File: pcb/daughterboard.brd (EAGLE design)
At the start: 28 x 24 mm, 26 parts, among them IC3 STM32F042F4, SW1 324_SW, SW2 324_SW, SW3 324_SW, SW4 324_SW, SW5 324_SW, SW6 324_SW, U4 XC6206_DEV

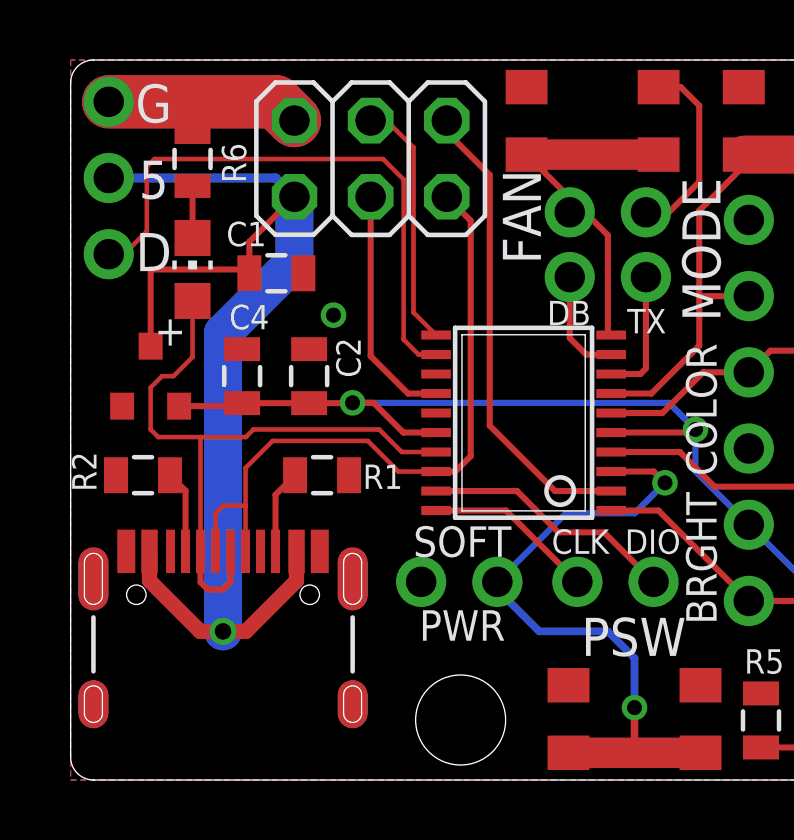
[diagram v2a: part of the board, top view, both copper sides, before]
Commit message: fixed a wrong signal
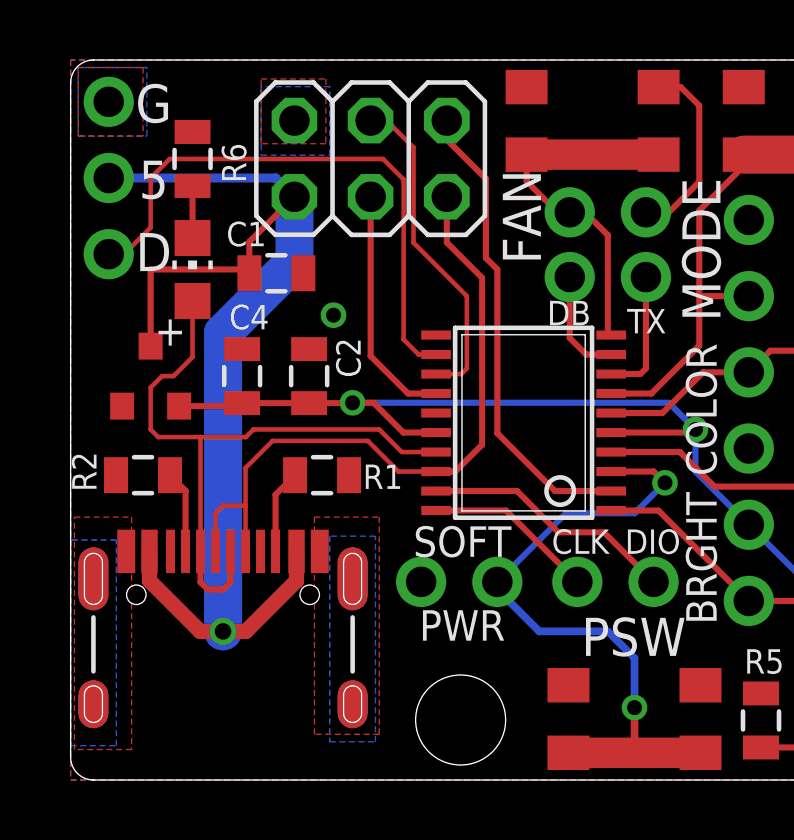
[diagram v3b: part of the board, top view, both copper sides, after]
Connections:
- net N$1: now also IC3.13; no longer IC3.11
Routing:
- net GND: track 19.2 -> 6.35 mm
- net N$1: track 8.36 -> 11.0 mm
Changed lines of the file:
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@@
 <contactref element="J4" pad="GND"/>
 <contactref element="JP3" pad="3"/>
-<wire x1="7.46" y1="21.98" x2="6.834" y2="22.606" width="1.778" layer="1"/>
-<wire x1="6.834" y1="22.606" x2="1.27" y2="22.606" width="1.778" layer="1"/>
-<wire x1="7.46" y1="21.98" x2="6.834" y2="22.606" width="1.778" layer="16"/>
-<wire x1="6.834" y1="22.606" x2="1.27" y2="22.606" width="1.778" layer="16"/>
 <contactref element="SW6" pad="P$3"/>
 <contactref element="SW6" pad="P$2"/>
@@
 </polygon>
 <via x="8.763" y="15.494" extent="1-16" drill="0.5"/>
+<polygon width="0.1524" layer="16" thermals="no">
+<vertex x="0.254" y="21.463"/>
+<vertex x="2.54" y="21.463"/>
+<vertex x="2.54" y="23.749"/>
+<vertex x="0.254" y="23.749"/>
+</polygon>
+<polygon width="0.1524" layer="16" thermals="no">
+<vertex x="6.35" y="20.828"/>
+<vertex x="8.636" y="20.828"/>
+<vertex x="8.636" y="23.114"/>
+<vertex x="6.35" y="23.114"/>
+</polygon>
+<polygon width="0.1524" layer="16" thermals="no">
+<vertex x="8.636" y="1.27"/>
+<vertex x="10.16" y="1.27"/>
+<vertex x="10.16" y="8.128"/>
+<vertex x="8.636" y="8.128"/>
+</polygon>
+<polygon width="0.1524" layer="16" thermals="no">
+<vertex x="0" y="1.143"/>
+<vertex x="1.524" y="1.143"/>
+<vertex x="1.524" y="8.001"/>
+<vertex x="0" y="8.001"/>
+</polygon>
+<polygon width="0.1524" layer="1" thermals="no">
+<vertex x="0.254" y="23.749"/>
+<vertex x="2.413" y="23.749"/>
+<vertex x="2.413" y="21.463"/>
+<vertex x="0.254" y="21.463"/>
+</polygon>
+<polygon width="0.1524" layer="1" thermals="no">
+<vertex x="6.35" y="23.368"/>
+<vertex x="8.509" y="23.368"/>
+<vertex x="8.509" y="21.209"/>
+<vertex x="6.35" y="21.209"/>
+</polygon>
+<polygon width="0.1524" layer="1" thermals="no">
+<vertex x="8.128" y="8.763"/>
+<vertex x="10.287" y="8.763"/>
+<vertex x="10.287" y="1.524"/>
+<vertex x="8.128" y="1.524"/>
+</polygon>
+<polygon width="0.1524" layer="1" thermals="no">
+<vertex x="0.127" y="8.763"/>
+<vertex x="2.032" y="8.763"/>
+<vertex x="2.032" y="1.016"/>
+<vertex x="0.127" y="1.016"/>
+</polygon>
 </signal>
 <signal name="+3V3">
@@
 <contactref element="J4" pad="B6" route="any" routetag="J1.D+"/>
 <contactref element="JP1" pad="5"/>
-<wire x1="12.54" y1="19.44" x2="13.335" y2="18.645" width="0.2032" layer="1"/>
+<wire x1="12.54" y1="19.44" x2="12.54" y2="17.916" width="0.2032" layer="1"/>
+<wire x1="13.716" y1="16.74" x2="12.54" y2="17.916" width="0.2032" layer="1"/>
 <wire x1="12.822" y1="10.282" x2="12.1812" y2="10.282" width="0.2032" layer="1"/>
-<wire x1="13.335" y1="18.645" x2="13.335" y2="10.795" width="0.2032" layer="1"/>
-<wire x1="13.335" y1="10.795" x2="12.822" y2="10.282" width="0.2032" layer="1"/>
+<wire x1="13.716" y1="16.74" x2="13.716" y2="11.176" width="0.2032" layer="1"/>
+<wire x1="13.716" y1="11.176" x2="12.822" y2="10.282" width="0.2032" layer="1"/>
 <wire x1="5.83" y1="7.62" x2="5.83" y2="9.144" width="0.1524" layer="1"/>
 <wire x1="5.83" y1="9.144" x2="5.83" y2="10.402" width="0.1524" layer="1"/>
@@
 <signal name="N$1">
 <contactref element="JP1" pad="4"/>
-<contactref element="IC3" pad="11"/>
-<wire x1="12.1812" y1="14.832" x2="11.43" y2="15.5832" width="0.1524" layer="1"/>
 <wire x1="10.532" y1="21.98" x2="10" y2="21.98" width="0.1524" layer="1"/>
-<wire x1="11.43" y1="15.5832" x2="11.43" y2="21.082" width="0.1524" layer="1"/>
-<wire x1="11.43" y1="21.082" x2="10.532" y2="21.98" width="0.1524" layer="1"/>
+<wire x1="10.532" y1="21.98" x2="11.43" y2="21.082" width="0.1524" layer="1"/>
+<contactref element="IC3" pad="13"/>
+<wire x1="11.43" y1="21.082" x2="11.43" y2="17.907" width="0.1524" layer="1"/>
+<wire x1="11.43" y1="17.907" x2="13.208" y2="16.129" width="0.1524" layer="1"/>
+<wire x1="13.208" y1="16.129" x2="13.208" y2="13.716" width="0.1524" layer="1"/>
+<wire x1="13.024" y1="13.532" x2="12.1812" y2="13.532" width="0.1524" layer="1"/>
+<wire x1="13.208" y1="13.716" x2="13.024" y2="13.532" width="0.1524" layer="1"/>
 </signal>
 <signal name="N$2">
@@
 <contactref element="JP1" pad="6"/>
 <contactref element="IC3" pad="2"/>
-<wire x1="18.0168" y1="9.632" x2="16.149" y2="9.632" width="0.2032" layer="1"/>
-<wire x1="16.149" y1="9.632" x2="13.97" y2="11.811" width="0.2032" layer="1"/>
-<wire x1="13.97" y1="11.811" x2="13.97" y2="20.169" width="0.2032" layer="1"/>
-<wire x1="13.97" y1="20.169" x2="12.54" y2="21.599" width="0.2032" layer="1"/>
-<wire x1="12.54" y1="21.599" x2="12.54" y2="21.98" width="0.2032" layer="1"/>
+<wire x1="16.149" y1="9.632" x2="18.0168" y2="9.632" width="0.2032" layer="1"/>
+<wire x1="13.843" y1="20.042" x2="12.54" y2="21.345" width="0.2032" layer="1"/>
+<wire x1="12.54" y1="21.345" x2="12.54" y2="21.98" width="0.2032" layer="1"/>
+<wire x1="13.843" y1="20.042" x2="13.843" y2="17.399" width="0.2032" layer="1"/>
+<wire x1="14.224" y1="11.557" x2="16.149" y2="9.632" width="0.2032" layer="1"/>
+<wire x1="13.843" y1="17.399" x2="14.224" y2="17.018" width="0.2032" layer="1"/>
+<wire x1="14.224" y1="17.018" x2="14.224" y2="11.557" width="0.2032" layer="1"/>
 </signal>
 <signal name="N$5">
@@
 <wire x1="11.0998" y1="14.6812" x2="11.0998" y2="20.0152" width="0.1524" layer="1"/>
 <wire x1="11.0998" y1="20.0152" x2="10.414" y2="20.701" width="0.1524" layer="1"/>
-<wire x1="10.414" y1="20.701" x2="2.794" y2="20.701" width="0.1524" layer="1"/>
-<wire x1="2.794" y1="20.701" x2="2.54" y2="20.447" width="0.1524" layer="1"/>
-<wire x1="2.54" y1="20.447" x2="2.54" y2="18.288" width="0.1524" layer="1"/>
-<wire x1="2.54" y1="18.288" x2="1.778" y2="17.526" width="0.1524" layer="1"/>
+<wire x1="10.414" y1="20.701" x2="3.302" y2="20.701" width="0.1524" layer="1"/>
+<wire x1="3.302" y1="20.701" x2="2.667" y2="20.066" width="0.1524" layer="1"/>
+<wire x1="2.667" y1="20.066" x2="2.667" y2="18.415" width="0.1524" layer="1"/>
+<wire x1="2.667" y1="18.415" x2="1.778" y2="17.526" width="0.1524" layer="1"/>
 <wire x1="1.778" y1="17.526" x2="1.27" y2="17.526" width="0.1524" layer="1"/>
 </signal>
@@
 <wire x1="17.907" y1="18.161" x2="17.145" y2="18.923" width="0.2032" layer="1"/>
 <wire x1="17.145" y1="18.923" x2="16.637" y2="18.923" width="0.2032" layer="1"/>
-<wire x1="16.637" y1="18.923" x2="16.637" y2="19.408" width="0.2032" layer="1"/>
-<wire x1="16.637" y1="19.408" x2="15.199" y2="20.846" width="0.2032" layer="1"/>
+<wire x1="16.637" y1="18.923" x2="16.233" y2="18.923" width="0.2032" layer="1"/>
+<wire x1="16.233" y1="18.923" x2="15.199" y2="19.957" width="0.2032" layer="1"/>
+<wire x1="15.199" y1="19.957" x2="15.199" y2="20.846" width="0.2032" layer="1"/>
 </signal>
 <signal name="N$10">

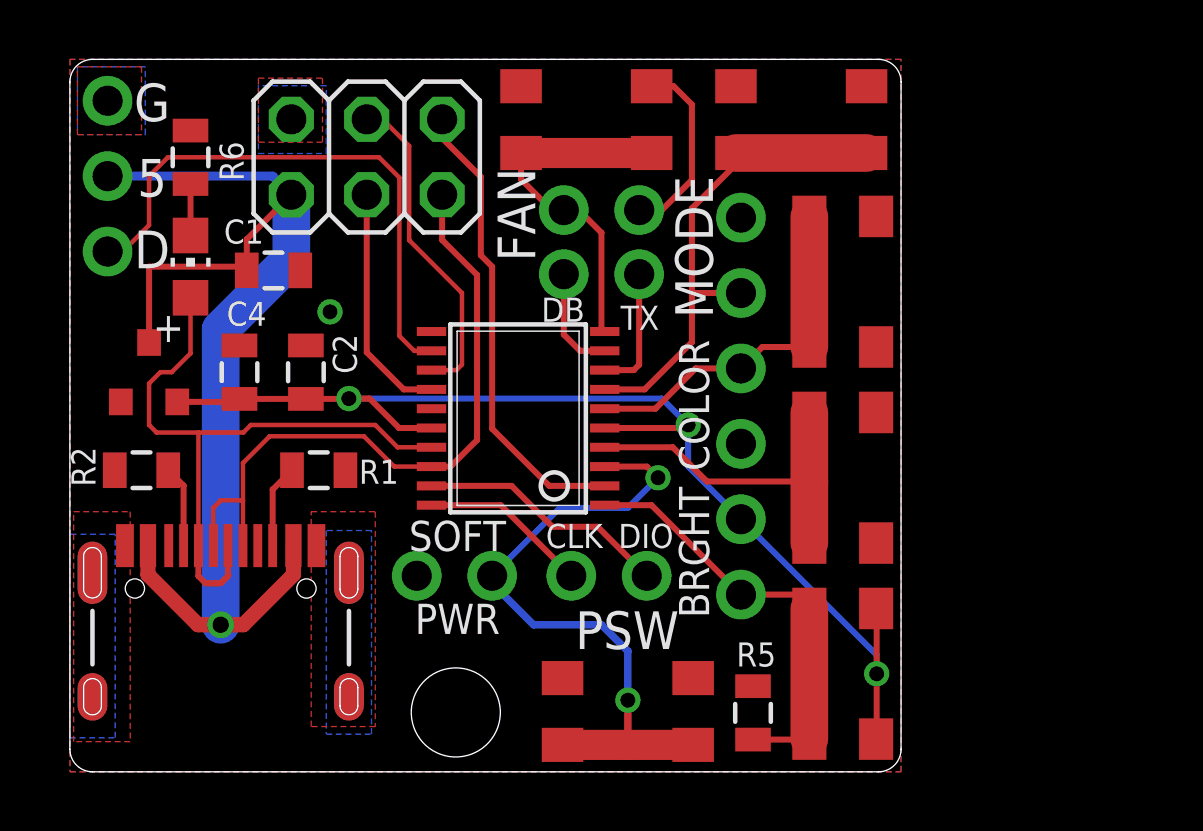
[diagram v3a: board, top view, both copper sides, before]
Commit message: added pullup on 1wire, gnd pour cleanup
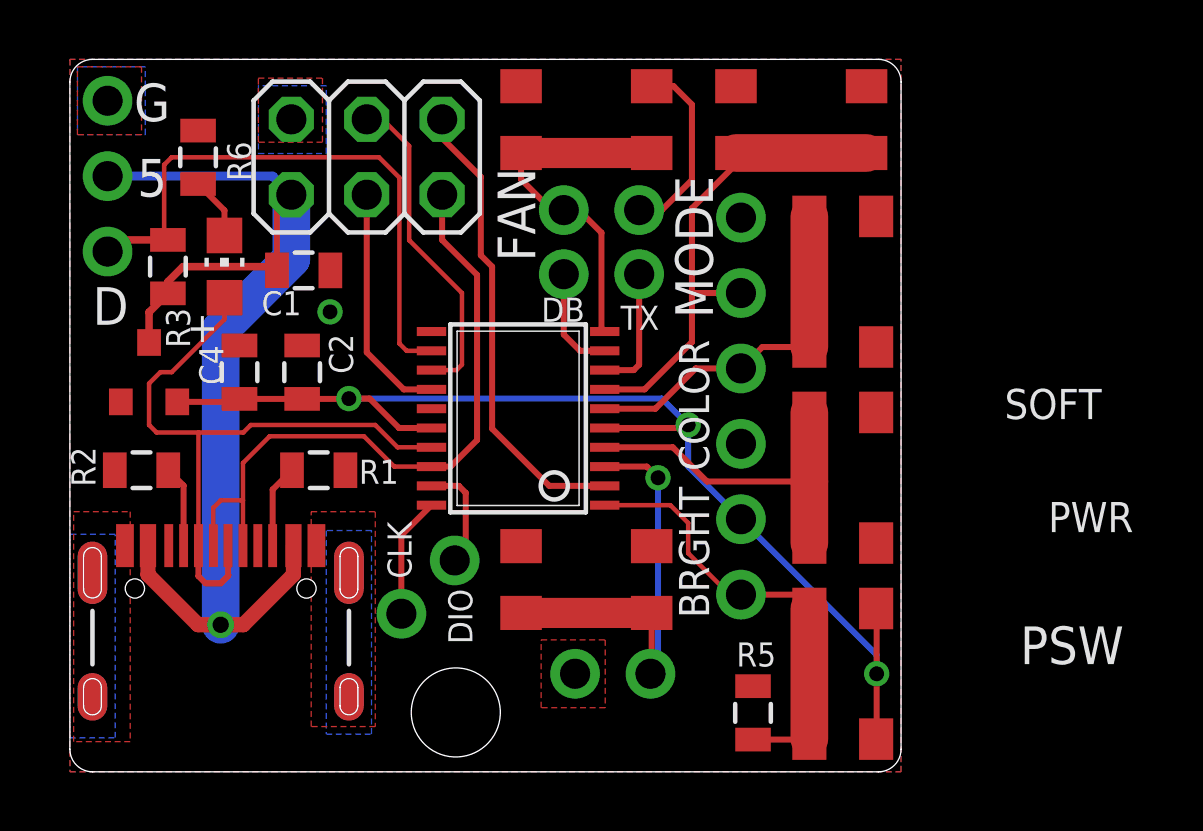
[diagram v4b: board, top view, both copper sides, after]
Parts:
- added R3: 5K1, SparkFun-Passives:0805
- R1, R2, R5: value 5.1K -> 5K1
- R6: value 1K -> 5K1
- moved U$7 6.27 mm to (18.3, 3.30)
- moved U$5 6.11 mm to (12.1, 6.22), turned to 45 degrees
- moved SW6 4.66 mm to (17.4, 6.48)
- moved LED2 1.14 mm to (5.21, 17.0)
- moved C1 1.02 mm to (7.87, 16.9)
- moved R6 0.25 mm to (4.32, 20.7)
- moved C2 0.13 mm to (7.82, 13.5)
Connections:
- net +5V: now also R3.1
- net N$5: now also R3.2
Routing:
- net N$12: track 22.2 -> 15.1 mm, vias 2 -> 1
- net N$3: track 8.50 -> 3.68 mm
- net N$4: track 5.69 -> 4.08 mm
- net N$5: track 19.0 -> 19.8 mm
- net BUTTON2: track 14.6 -> 15.2 mm

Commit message: cleanup
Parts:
- removed SW3: 324_SW, 3pos_slide_switch_centered:342_SWICH_FOOT
- added U$8: PINHD1X2, adafruit_changed:1X02
- moved SW4 3.68 mm to (26.0, 6.99), turned to 270 degrees
- moved R5 3.14 mm to (26.0, 2.82), turned to 180 degrees
- moved U$4 0.51 mm to (22.6, 6.73)
- moved U$5 0.28 mm to (12.2, 6.48)
- moved U$3 0.25 mm to (22.6, 12.1)
- moved U$7 0.25 mm to (18.3, 3.05)
- moved SW6 0.13 mm to (17.4, 6.35)
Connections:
- net BUTTON1: now also U$8.1; no longer SW3.P$2, SW3.P$3
- net GND: now also U$8.2; no longer SW3.P$1, SW3.P$4
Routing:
- net +3V3: track 39.1 -> 35.3 mm, vias 3 -> 2
- net BUTTON2: track 15.2 -> 18.2 mm
- net BUTTON1: track 11.8 -> 9.00 mm
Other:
- board text added: "ATX4VC MCU Board"
- board text added: "DFU"
- board text added: "PD1 APR23"
- board text added: "SOFT PWR"
- board text removed: "ATX4VC Expansion Card"
- board text removed: "PSW"
- board text removed: "PT1 APR23"
- board text removed: "PWR"
- board text removed: "SOFT"

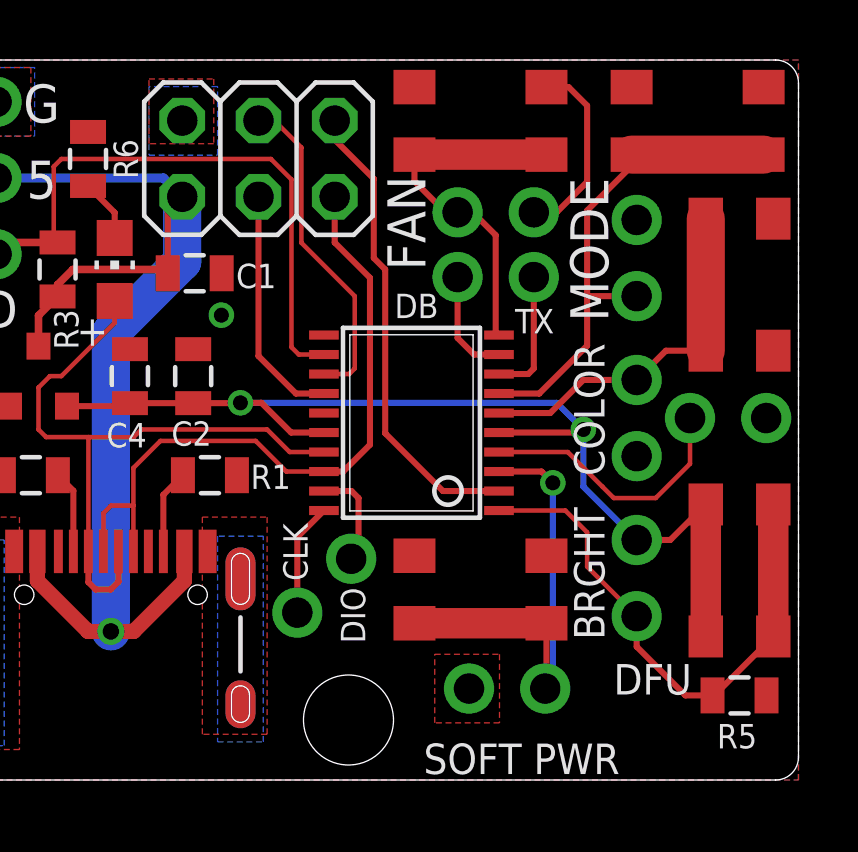
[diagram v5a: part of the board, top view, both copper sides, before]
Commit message: moved pin headers to the outer edge
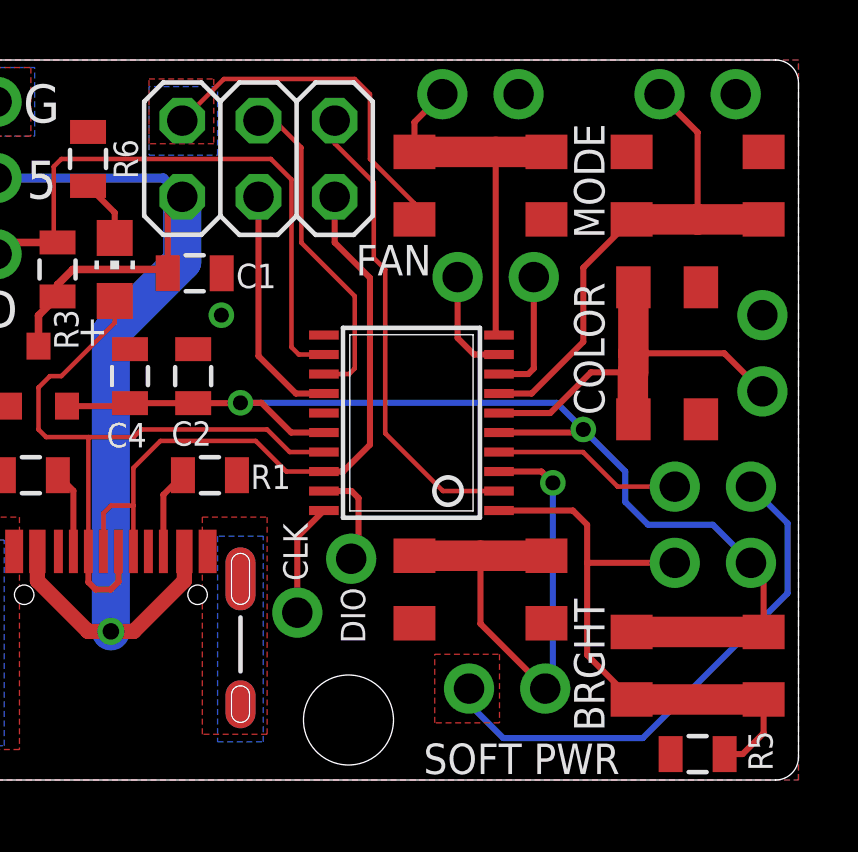
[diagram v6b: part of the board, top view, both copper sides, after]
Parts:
- moved U$2 5.83 mm to (24.6, 22.9), turned to 0 degrees
- moved U$3 4.71 mm to (26.8, 14.2), turned to 90 degrees
- moved U$1 3.97 mm to (17.4, 22.9)
- moved SW4 3.47 mm to (24.6, 3.81), turned to 180 degrees
- moved SW5 3.32 mm to (23.6, 14.2)
- moved U$4 2.59 mm to (25.1, 7.24), turned to 180 degrees
- moved R5 2.40 mm to (24.6, 0.86), turned to 0 degrees
- moved U$8 2.34 mm to (25.1, 9.78)
- moved SW1 2.16 mm to (17.4, 19.8), turned to 0 degrees
- moved SW2 2.16 mm to (24.6, 19.8)
- turned SW6 to 180 degrees
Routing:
- net GND: track 6.35 -> 29.5 mm
- net +3V3: track 35.3 -> 38.6 mm
- net N$12: track 15.5 -> 18.6 mm
- net BUTTON1: track 9.00 -> 6.34 mm
- net N$11: track 12.2 -> 14.3 mm
- net BUTTON2: track 18.2 -> 19.6 mm
- net N$9: track 12.1 -> 12.9 mm
- net N$10: track 16.6 -> 17.4 mm
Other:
- board text removed: "DFU"
